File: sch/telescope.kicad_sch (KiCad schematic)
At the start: 79 parts, among them J1 USB_B, J2 M1, J3 M2, J4 12V, J5 UART, J6 AUX, Q1 MMBT3904, Q2 MMBT3904, Q3 MMBT3904, Q4 MMBT3904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

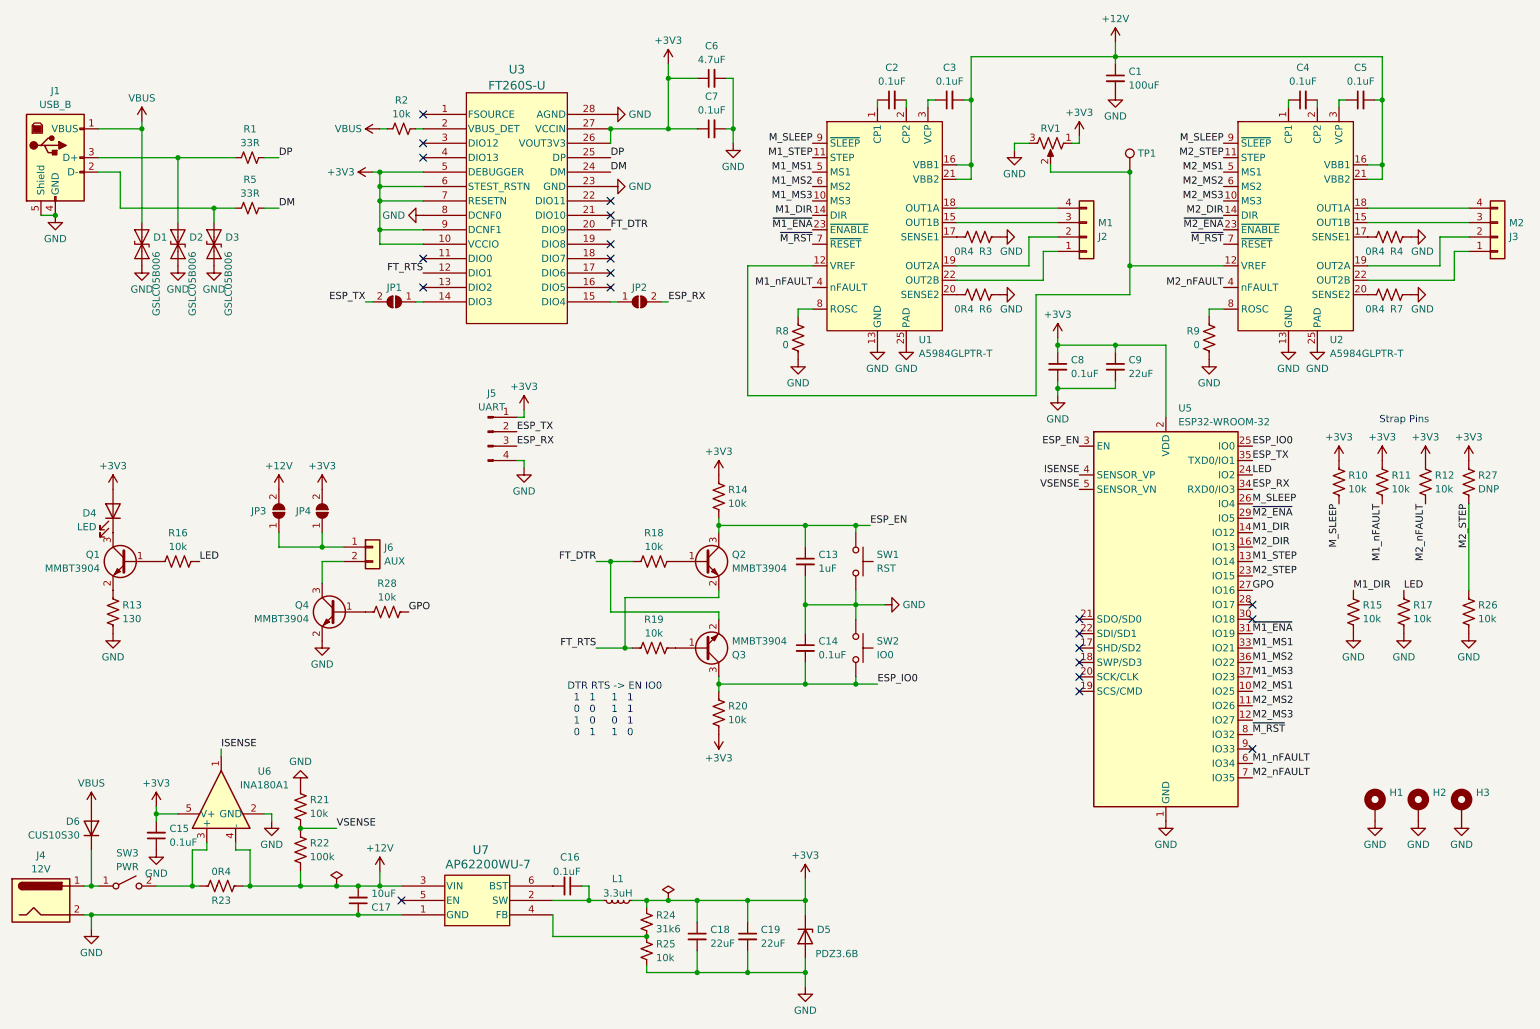
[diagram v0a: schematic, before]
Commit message: add reset control pull down
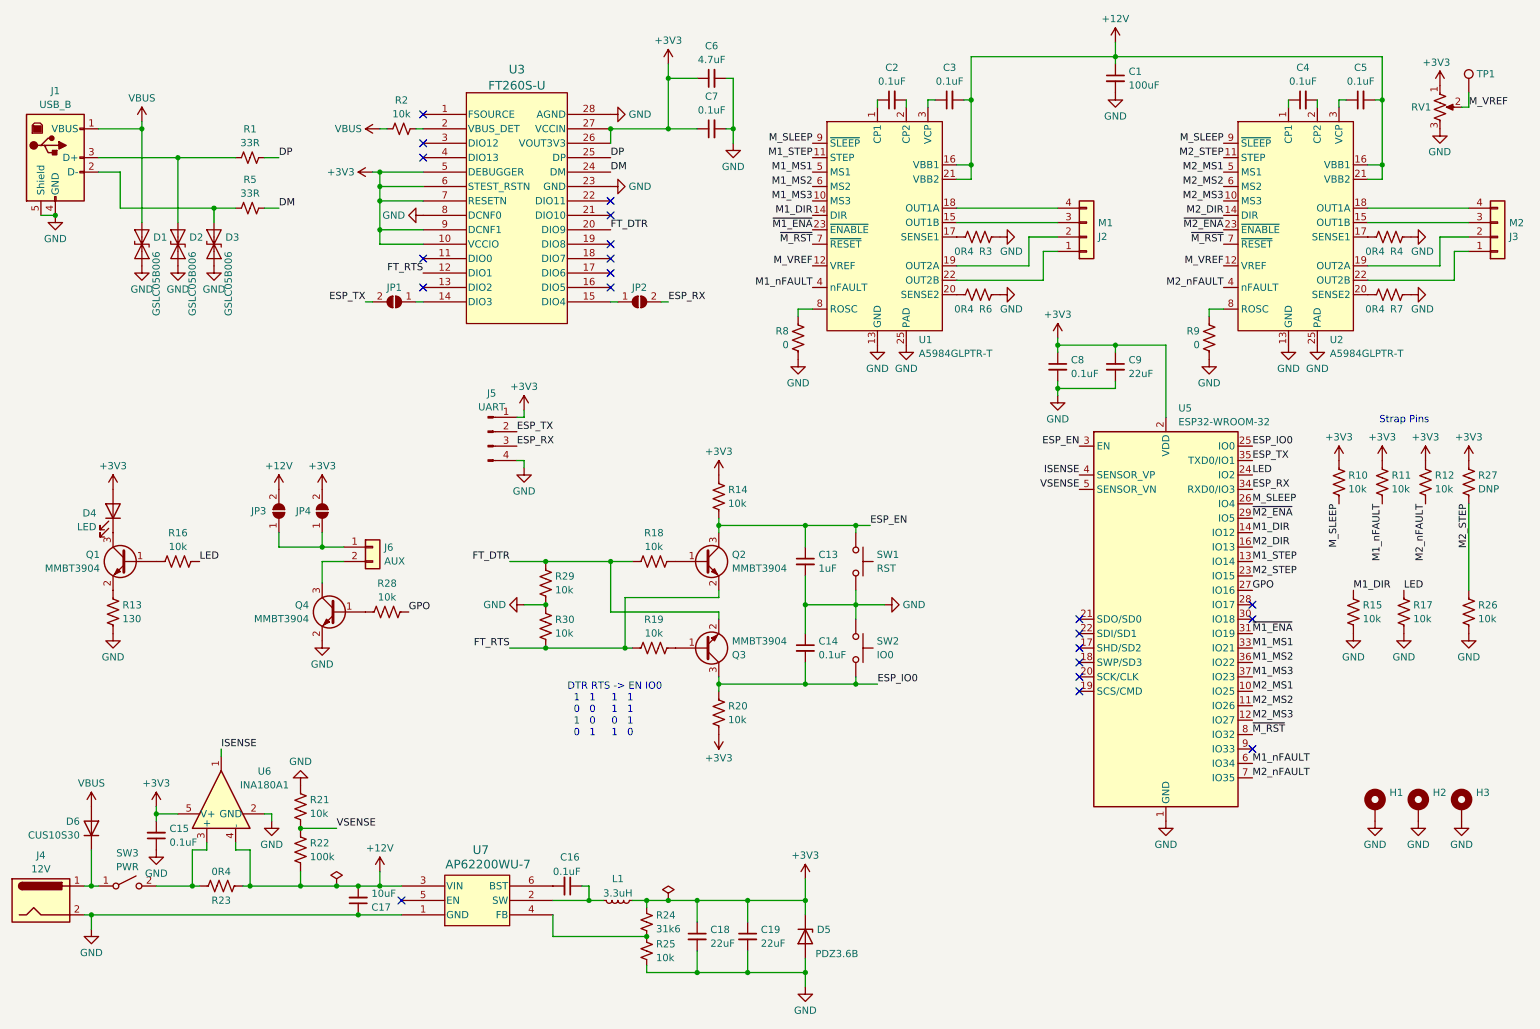
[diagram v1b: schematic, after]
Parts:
- added R29, R30: 10k, Resistor_SMD:R_0805_2012Metric_Pad1.20x1.40mm_HandSolder, symbol Device:R_US
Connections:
- net FT_DTR: now also R29.2
- net FT_RTS: now also R30.1
- net GND: now also R29.1, R30.2
- net M_VREF: now reaches RV1.2, TP1.1, U1.12 (VREF), U2.12 (VREF)
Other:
- moved on the sheet: RV1, TP1
